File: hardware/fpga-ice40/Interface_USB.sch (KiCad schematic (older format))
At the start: 12 parts, among them J5 USB_B_Micro, U7 FT245RL

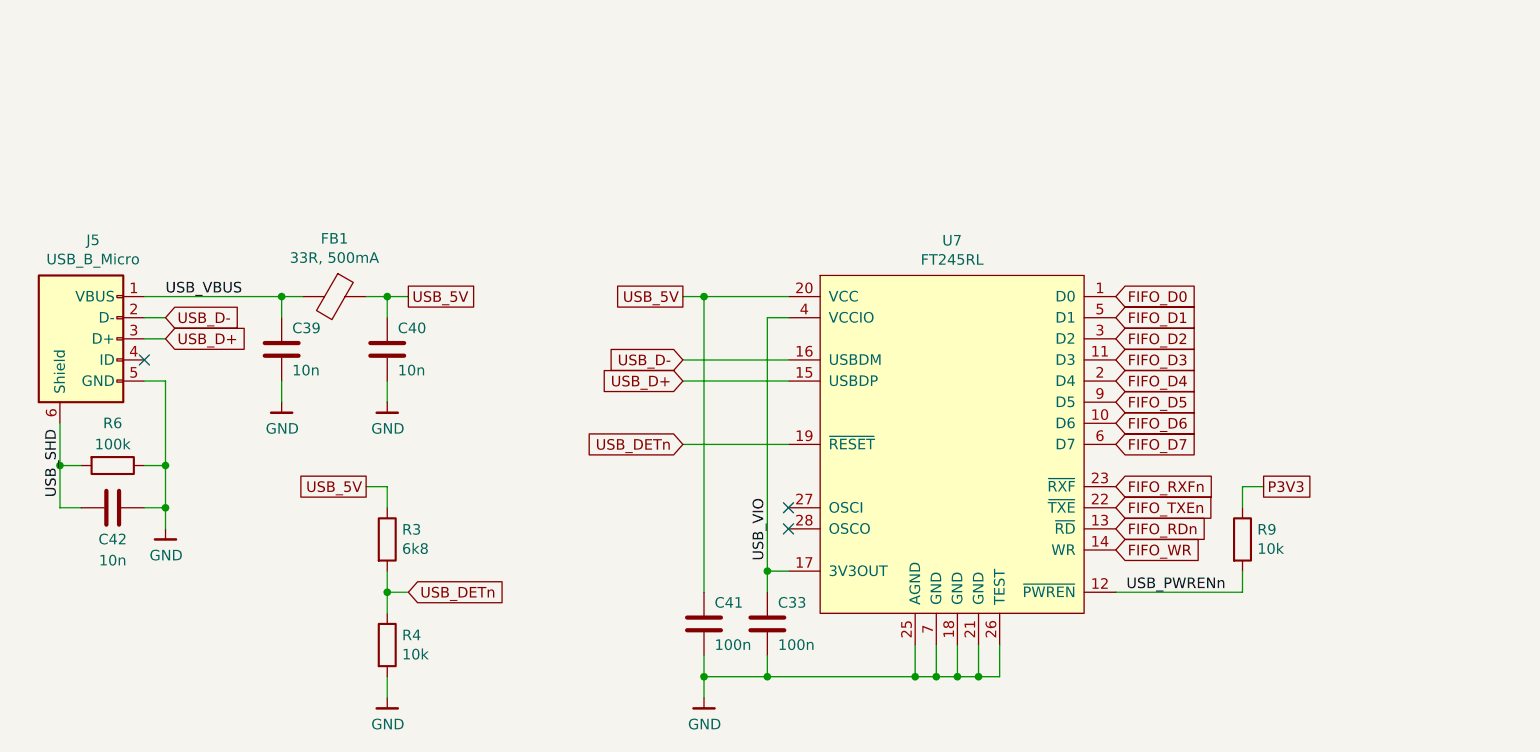
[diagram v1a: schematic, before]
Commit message: Reannotate schematic symbols
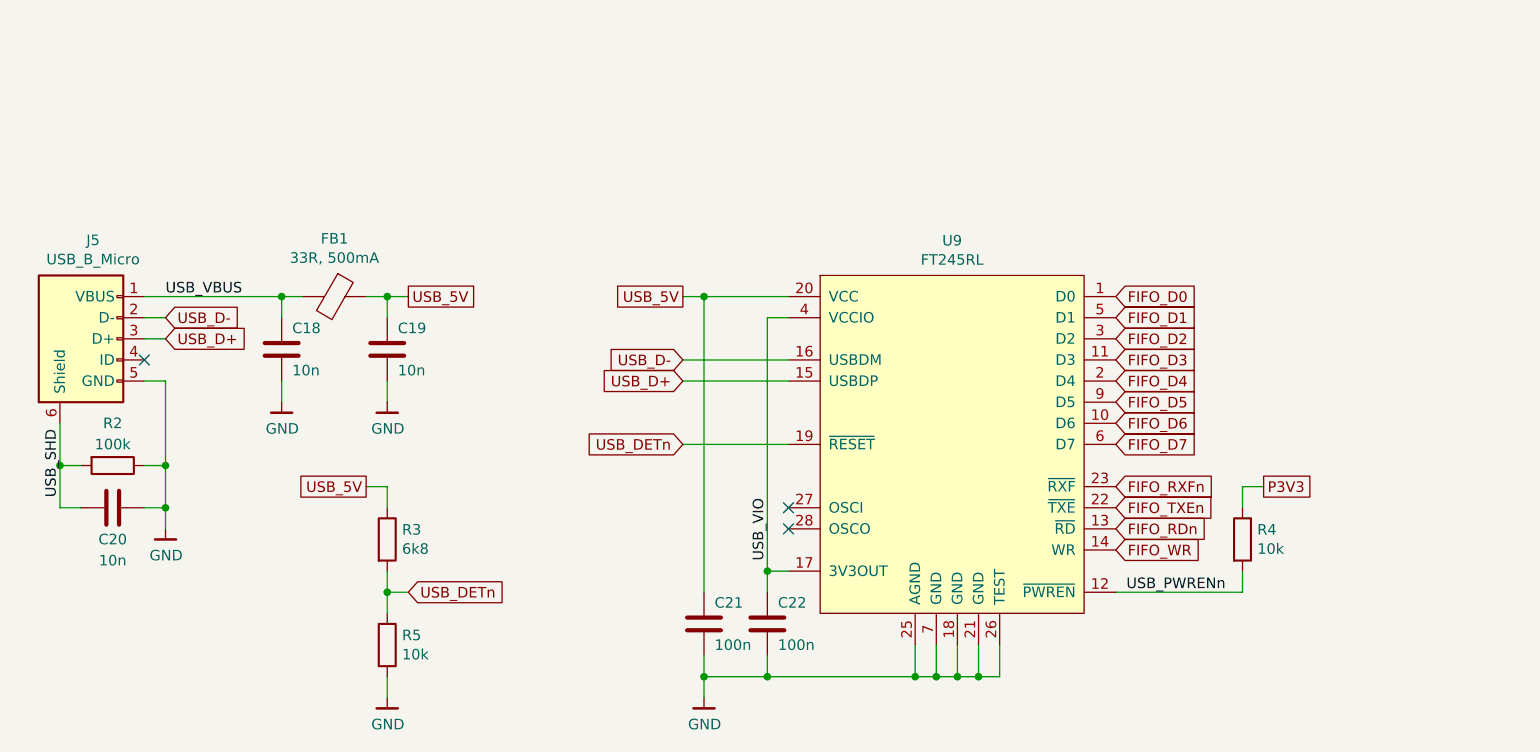
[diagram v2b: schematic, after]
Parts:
- renumbered C39 to C18, C40 to C19, C42 to C20, C41 to C21, C33 to C22, R6 to R2, R9 to R4, R4 to R5, U7 to U9
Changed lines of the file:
@@
 P 6350 3750
 AR Path="/5F314850" Ref="U?"  Part="1"
-AR Path="/5F302051/5F314850" Ref="U7"  Part="1"
-F 0 "U7" H 6975 4315 50  0000 C CNN
+AR Path="/5F302051/5F314850" Ref="U9"  Part="1"
+F 0 "U9" H 6975 4315 50  0000 C CNN
 F 1 "FT245RL" H 6975 4224 50  0000 C CNN
 F 2 "Package_SO:SSOP-28_5.3x10.2mm_P0.65mm" H 6500 4200 50  0001 C CNN
@@
 P 5800 5350
 AR Path="/5F314866" Ref="#PWR?"  Part="1"
-AR Path="/5F302051/5F314866" Ref="#PWR0121"  Part="1"
-F 0 "#PWR0121" H 5800 5100 50  0001 C CNN
+AR Path="/5F302051/5F314866" Ref="#PWR025"  Part="1"
+F 0 "#PWR025" H 5800 5100 50  0001 C CNN
 F 1 "GND" H 5803 5224 50  0000 C CNN
 F 2 "" H 5700 5000 50  0001 C CNN
@@
 P 6100 5000
 AR Path="/5F31486F" Ref="C?"  Part="1"
-AR Path="/5F302051/5F31486F" Ref="C33"  Part="1"
-F 0 "C33" H 6150 5100 50  0000 L CNN
+AR Path="/5F302051/5F31486F" Ref="C22"  Part="1"
+F 0 "C22" H 6150 5100 50  0000 L CNN
 F 1 "100n" H 6150 4900 50  0000 L CNN
 F 2 "Capacitor_SMD:C_0603_1608Metric" H 6138 4850 50  0001 C CNN
@@
 P 8350 4600
 AR Path="/5F314883" Ref="R?"  Part="1"
-AR Path="/5F302051/5F314883" Ref="R9"  Part="1"
-F 0 "R9" H 8420 4646 50  0000 L CNN
+AR Path="/5F302051/5F314883" Ref="R4"  Part="1"
+F 0 "R4" H 8420 4646 50  0000 L CNN
 F 1 "10k" H 8420 4555 50  0000 L CNN
 F 2 "Resistor_SMD:R_0603_1608Metric" V 8280 4600 50  0001 C CNN
@@
 P 3250 4550
 AR Path="/5F3148A5" Ref="#PWR?"  Part="1"
-AR Path="/5F302051/5F3148A5" Ref="#PWR0122"  Part="1"
-F 0 "#PWR0122" H 3250 4300 50  0001 C CNN
+AR Path="/5F302051/5F3148A5" Ref="#PWR023"  Part="1"
+F 0 "#PWR023" H 3250 4300 50  0001 C CNN
 F 1 "GND" H 3253 4424 50  0000 C CNN
 F 2 "" H 3150 4200 50  0001 C CNN
@@
 P 4300 5100
 AR Path="/5F3148B3" Ref="R?"  Part="1"
-AR Path="/5F302051/5F3148B3" Ref="R4"  Part="1"
-F 0 "R4" H 4370 5146 50  0000 L CNN
+AR Path="/5F302051/5F3148B3" Ref="R5"  Part="1"
+F 0 "R5" H 4370 5146 50  0000 L CNN
 F 1 "10k" H 4370 5055 50  0000 L CNN
 F 2 "Resistor_SMD:R_0603_1608Metric" V 4230 5100 50  0001 C CNN
@@
 P 4300 5350
 AR Path="/5F3148BA" Ref="#PWR?"  Part="1"
-AR Path="/5F302051/5F3148BA" Ref="#PWR0123"  Part="1"
-F 0 "#PWR0123" H 4300 5100 50  0001 C CNN
+AR Path="/5F302051/5F3148BA" Ref="#PWR024"  Part="1"
+F 0 "#PWR024" H 4300 5100 50  0001 C CNN
 F 1 "GND" H 4303 5224 50  0000 C CNN
 F 2 "" H 4200 5000 50  0001 C CNN
@@
 P 5800 5000
 AR Path="/5F3148C7" Ref="C?"  Part="1"
-AR Path="/5F302051/5F3148C7" Ref="C41"  Part="1"
-F 0 "C41" H 5850 5100 50  0000 L CNN
+AR Path="/5F302051/5F3148C7" Ref="C21"  Part="1"
+F 0 "C21" H 5850 5100 50  0000 L CNN
 F 1 "100n" H 5850 4900 50  0000 L CNN
 F 2 "Capacitor_SMD:C_0603_1608Metric" H 5838 4850 50  0001 C CNN
@@
 P 3800 3700
 AR Path="/5F3148D5" Ref="C?"  Part="1"
-AR Path="/5F302051/5F3148D5" Ref="C39"  Part="1"
-F 0 "C39" H 3850 3800 50  0000 L CNN
+AR Path="/5F302051/5F3148D5" Ref="C18"  Part="1"
+F 0 "C18" H 3850 3800 50  0000 L CNN
 F 1 "10n" H 3850 3600 50  0000 L CNN
 F 2 "Capacitor_SMD:C_0603_1608Metric" H 3838 3550 50  0001 C CNN
@@
 P 3800 3950
 AR Path="/5F3148DE" Ref="#PWR?"  Part="1"
-AR Path="/5F302051/5F3148DE" Ref="#PWR0124"  Part="1"
-F 0 "#PWR0124" H 3800 3700 50  0001 C CNN
+AR Path="/5F302051/5F3148DE" Ref="#PWR021"  Part="1"
+F 0 "#PWR021" H 3800 3700 50  0001 C CNN
 F 1 "GND" H 3803 3824 50  0000 C CNN
 F 2 "" H 3700 3600 50  0001 C CNN
@@
 P 4300 3700
 AR Path="/5F3148ED" Ref="C?"  Part="1"
-AR Path="/5F302051/5F3148ED" Ref="C40"  Part="1"
-F 0 "C40" H 4350 3800 50  0000 L CNN
+AR Path="/5F302051/5F3148ED" Ref="C19"  Part="1"
+F 0 "C19" H 4350 3800 50  0000 L CNN
 F 1 "10n" H 4350 3600 50  0000 L CNN
 F 2 "Capacitor_SMD:C_0603_1608Metric" H 4338 3550 50  0001 C CNN
@@
 P 4300 3950
 AR Path="/5F3148F5" Ref="#PWR?"  Part="1"
-AR Path="/5F302051/5F3148F5" Ref="#PWR0125"  Part="1"
-F 0 "#PWR0125" H 4300 3700 50  0001 C CNN
+AR Path="/5F302051/5F3148F5" Ref="#PWR022"  Part="1"
+F 0 "#PWR022" H 4300 3700 50  0001 C CNN
 F 1 "GND" H 4303 3824 50  0000 C CNN
 F 2 "" H 4200 3600 50  0001 C CNN
@@
 P 3000 4250
 AR Path="/5F314900" Ref="R?"  Part="1"
-AR Path="/5F302051/5F314900" Ref="R6"  Part="1"
-F 0 "R6" V 2800 4250 50  0000 C CNN
+AR Path="/5F302051/5F314900" Ref="R2"  Part="1"
+F 0 "R2" V 2800 4250 50  0000 C CNN
 F 1 "100k" V 2900 4250 50  0000 C CNN
 F 2 "Resistor_SMD:R_0603_1608Metric" V 2930 4250 50  0001 C CNN
@@
 P 3000 4450
 AR Path="/5F314906" Ref="C?"  Part="1"
-AR Path="/5F302051/5F314906" Ref="C42"  Part="1"
-F 0 "C42" V 2850 4450 50  0000 C CNN
+AR Path="/5F302051/5F314906" Ref="C20"  Part="1"
+F 0 "C20" V 2850 4450 50  0000 C CNN
 F 1 "10n" V 2750 4450 50  0000 C CNN
 F 2 "Capacitor_SMD:C_0603_1608Metric" H 3038 4300 50  0001 C CNN

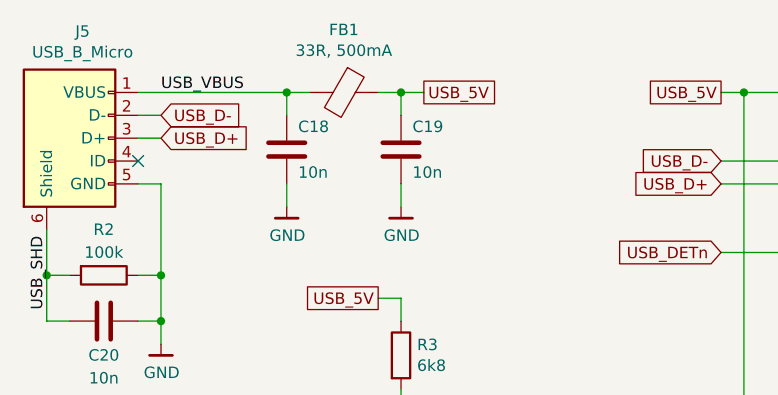
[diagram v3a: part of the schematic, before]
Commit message: Component selection by MPN and routing cleanup
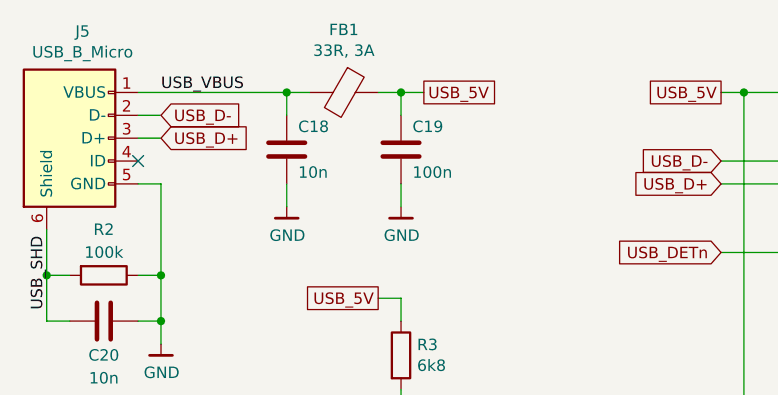
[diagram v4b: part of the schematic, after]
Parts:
- C18, C20: MPN (none) -> CL10B103KC8NNNC
- C19: value 10n -> 100n; MPN (none) -> CL10B104KB8NNNC
- C21, C22: MPN (none) -> CL10B104KB8NNNC
- FB1: value 33R, 500mA -> 33R, 3A; MPN 742792605 -> BLM18PG330SN1D
- J5: MPN (none) -> 47346-0001
- U9: MPN (none) -> FT245RL-REEL
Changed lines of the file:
@@
 F 2 "Package_SO:SSOP-28_5.3x10.2mm_P0.65mm" H 6500 4200 50  0001 C CNN
 F 3 "https://www.ftdichip.com/Support/Documents/DataSheets/ICs/DS_FT245R.pdf" H 6500 4200 50  0001 C CNN
+F 4 "FT245RL-REEL" H 6350 3750 50  0001 C CNN "MPN"
 	1    6350 3750
 	1    0    0    -1
@@
 F 2 "Capacitor_SMD:C_0603_1608Metric" H 6138 4850 50  0001 C CNN
 F 3 "~" H 6100 5000 50  0001 C CNN
+F 4 "CL10B104KB8NNNC" H 6100 5000 50  0001 C CNN "MPN"
 	1    6100 5000
 	1    0    0    -1
@@
 Text Label 7800 4850 0    50   ~ 0
 USB_PWRENn
-NoConn ~ 3150 3750
-Wire Wire Line
-	3150 3850 3250 3850
-Wire Wire Line
-	3250 3850 3250 4250
-Wire Wire Line
-	3150 3450 3800 3450
-Wire Wire Line
-	3150 3550 3250 3550
-Wire Wire Line
-	3150 3650 3250 3650
-$Comp
-L ng_power:GND #PWR?
-U 1 1 5F3148A5
-P 3250 4550
-AR Path="/5F3148A5" Ref="#PWR?"  Part="1"
-AR Path="/5F302051/5F3148A5" Ref="#PWR023"  Part="1"
-F 0 "#PWR023" H 3250 4300 50  0001 C CNN
-F 1 "GND" H 3253 4424 50  0000 C CNN
-F 2 "" H 3150 4200 50  0001 C CNN
-F 3 "" H 3250 4550 50  0001 C CNN
-	1    3250 4550
-	1    0    0    -1
-$EndComp
-Text GLabel 3250 3550 2    50   Input ~ 0
-USB_D-
-Text GLabel 3250 3650 2    50   Input ~ 0
-USB_D+
 $Comp
 L Device:R R?
@@
 F 2 "Capacitor_SMD:C_0603_1608Metric" H 5838 4850 50  0001 C CNN
 F 3 "~" H 5800 5000 50  0001 C CNN
+F 4 "CL10B104KB8NNNC" H 5800 5000 50  0001 C CNN "MPN"
 	1    5800 5000
 	1    0    0    -1
@@
 F 2 "Capacitor_SMD:C_0603_1608Metric" H 3838 3550 50  0001 C CNN
 F 3 "~" H 3800 3700 50  0001 C CNN
+F 4 "CL10B103KC8NNNC" H 3800 3700 50  0001 C CNN "MPN"
 	1    3800 3700
 	1    0    0    -1
 $EndComp
-Text Label 3250 3450 0    50   ~ 0
-USB_VBUS
 Wire Wire Line
 	3800 3450 3800 3550
@@
 AR Path="/5F302051/5F3148E5" Ref="FB1"  Part="1"
 F 0 "FB1" V 3776 3450 50  0000 C CNN
-F 1 "33R, 500mA" V 3867 3450 50  0000 C CNN
+F 1 "33R, 3A" V 3867 3450 50  0000 C CNN
 F 2 "Inductor_SMD:L_0603_1608Metric" V 3980 3450 50  0001 C CNN
 F 3 "~" H 4050 3450 50  0001 C CNN
-F 4 "742792605" V 4050 3450 50  0001 C CNN "MPN"
+F 4 "BLM18PG330SN1D" V 4050 3450 50  0001 C CNN "MPN"
 	1    4050 3450
 	0    1    1    0
@@
 Wire Wire Line
 	3900 3450 3800 3450
-Connection ~ 3800 3450
 $Comp
 L Device:C C?
@@
 AR Path="/5F302051/5F3148ED" Ref="C19"  Part="1"
 F 0 "C19" H 4350 3800 50  0000 L CNN
-F 1 "10n" H 4350 3600 50  0000 L CNN
+F 1 "100n" H 4350 3600 50  0000 L CNN
 F 2 "Capacitor_SMD:C_0603_1608Metric" H 4338 3550 50  0001 C CNN
 F 3 "~" H 4300 3700 50  0001 C CNN
+F 4 "CL10B104KB8NNNC" H 4300 3700 50  0001 C CNN "MPN"
 	1    4300 3700
 	1    0    0    -1
@@
 Text GLabel 4200 4350 0    50   UnSpc ~ 0
 USB_5V
+Connection ~ 3800 3450
+$Comp
+L ng_conn:USB_B_Micro J?
+U 1 1 5F314899
+P 2850 3650
+AR Path="/5F314899" Ref="J?"  Part="1"
+AR Path="/5F302051/5F314899" Ref="J5"  Part="1"
+F 0 "J5" H 2907 4117 50  0000 C CNN
+F 1 "USB_B_Micro" H 2907 4026 50  0000 C CNN
+F 2 "Connector_USB:USB_Micro-B_Molex_47346-0001" H 3000 3650 50  0001 C CNN
+F 3 "~" H 3000 3650 50  0001 C CNN
+F 4 "47346-0001" H 2850 3650 50  0001 C CNN "MPN"
+	1    2850 3650
+	1    0    0    -1
+$EndComp
+Text Label 2750 4400 1    50   ~ 0
+USB_SHD
+Connection ~ 2750 4250
+Wire Wire Line
+	2750 4450 2750 4250
+Wire Wire Line
+	2850 4450 2750 4450
+Wire Wire Line
+	2750 4250 2750 4050
+Wire Wire Line
+	2850 4250 2750 4250
+Wire Wire Line
+	3250 4450 3250 4550
+Connection ~ 3250 4450
+Wire Wire Line
+	3150 4450 3250 4450
+Wire Wire Line
+	3250 4250 3250 4450
+Connection ~ 3250 4250
+Wire Wire Line
+	3150 4250 3250 4250
+$Comp
+L Device:C C?
+U 1 1 5F314906
+P 3000 4450
+AR Path="/5F314906" Ref="C?"  Part="1"
+AR Path="/5F302051/5F314906" Ref="C20"  Part="1"
+F 0 "C20" V 2850 4450 50  0000 C CNN
+F 1 "10n" V 2750 4450 50  0000 C CNN
+F 2 "Capacitor_SMD:C_0603_1608Metric" H 3038 4300 50  0001 C CNN
+F 3 "~" H 3000 4450 50  0001 C CNN
+F 4 "CL10B103KC8NNNC" H 3000 4450 50  0001 C CNN "MPN"
+	1    3000 4450
+	0    -1   -1   0
+$EndComp
 $Comp
 L Device:R R?
@@
 	0    1    1    0
 $EndComp
-$Comp
-L Device:C C?
-U 1 1 5F314906
-P 3000 4450
-AR Path="/5F314906" Ref="C?"  Part="1"
-AR Path="/5F302051/5F314906" Ref="C20"  Part="1"
-F 0 "C20" V 2850 4450 50  0000 C CNN
-F 1 "10n" V 2750 4450 50  0000 C CNN
-F 2 "Capacitor_SMD:C_0603_1608Metric" H 3038 4300 50  0001 C CNN
-F 3 "~" H 3000 4450 50  0001 C CNN
-	1    3000 4450
-	0    -1   -1   0
-$EndComp
-Wire Wire Line
-	3150 4250 3250 4250
-Connection ~ 3250 4250
-Wire Wire Line
-	3250 4250 3250 4450
-Wire Wire Line
-	3150 4450 3250 4450
-Connection ~ 3250 4450
-Wire Wire Line
-	3250 4450 3250 4550
-Wire Wire Line
-	2850 4250 2750 4250
-Wire Wire Line
-	2750 4250 2750 4050
-Wire Wire Line
-	2850 4450 2750 4450
-Wire Wire Line
-	2750 4450 2750 4250
-Connection ~ 2750 4250
-Text Label 2750 4400 1    50   ~ 0
-USB_SHD
-$Comp
-L ng_conn:USB_B_Micro J?
-U 1 1 5F314899
-P 2850 3650
-AR Path="/5F314899" Ref="J?"  Part="1"
-AR Path="/5F302051/5F314899" Ref="J5"  Part="1"
-F 0 "J5" H 2907 4117 50  0000 C CNN
-F 1 "USB_B_Micro" H 2907 4026 50  0000 C CNN
-F 2 "Connector_USB:USB_Micro-B_Molex_47346-0001" H 3000 3650 50  0001 C CNN
-F 3 "~" H 3000 3650 50  0001 C CNN
-	1    2850 3650
-	1    0    0    -1
-$EndComp
+Text Label 3250 3450 0    50   ~ 0
+USB_VBUS
+Text GLabel 3250 3650 2    50   Input ~ 0
+USB_D+
+Text GLabel 3250 3550 2    50   Input ~ 0
+USB_D-
+$Comp
+L ng_power:GND #PWR?
+U 1 1 5F3148A5
+P 3250 4550
+AR Path="/5F3148A5" Ref="#PWR?"  Part="1"
+AR Path="/5F302051/5F3148A5" Ref="#PWR023"  Part="1"
+F 0 "#PWR023" H 3250 4300 50  0001 C CNN
+F 1 "GND" H 3253 4424 50  0000 C CNN
+F 2 "" H 3150 4200 50  0001 C CNN
+F 3 "" H 3250 4550 50  0001 C CNN
+	1    3250 4550
+	1    0    0    -1
+$EndComp
+Wire Wire Line
+	3150 3650 3250 3650
+Wire Wire Line
+	3150 3550 3250 3550
+Wire Wire Line
+	3150 3450 3800 3450
+Wire Wire Line
+	3250 3850 3250 4250
+Wire Wire Line
+	3150 3850 3250 3850
+NoConn ~ 3150 3750
 $EndSCHEMATC

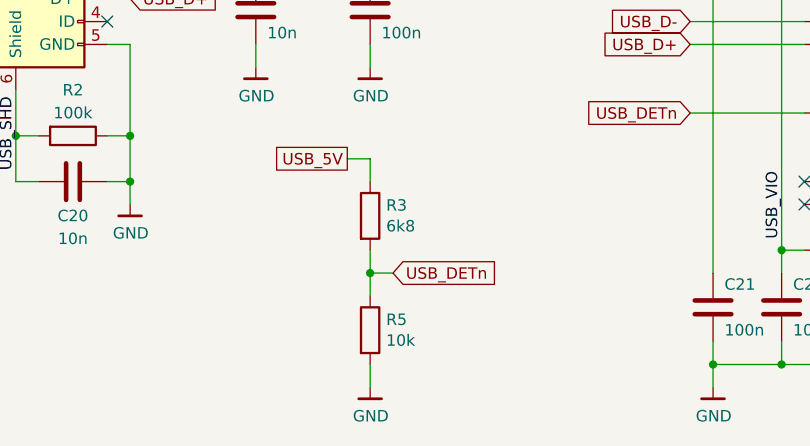
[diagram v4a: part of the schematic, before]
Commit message: Complete component selection by MPN
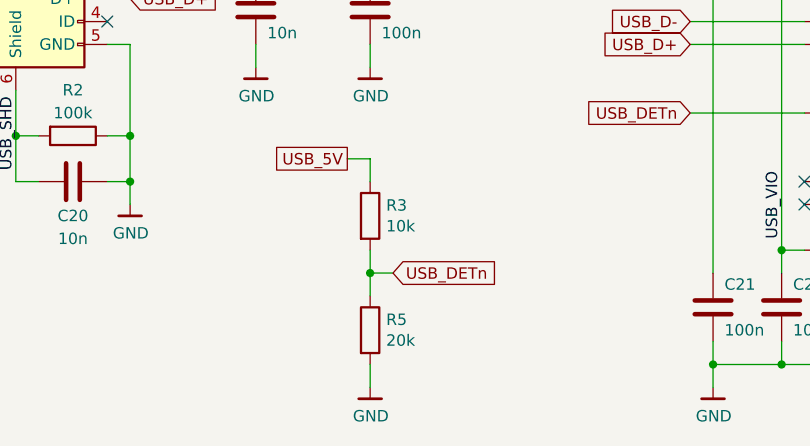
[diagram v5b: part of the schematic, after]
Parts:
- R2: MPN (none) -> RC0603JR-07100KL
- R3: value 6k8 -> 10k; MPN (none) -> RC0603FR-0710KL
- R4: MPN (none) -> RC0603FR-0710KL
- R5: value 10k -> 20k; MPN (none) -> RC0603JR-0720KL
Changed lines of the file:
@@
 F 2 "Resistor_SMD:R_0603_1608Metric" V 8280 4600 50  0001 C CNN
 F 3 "~" H 8350 4600 50  0001 C CNN
+F 4 "RC0603FR-0710KL" H 8350 4600 50  0001 C CNN "MPN"
 	1    8350 4600
 	1    0    0    -1
@@
 AR Path="/5F302051/5F3148AD" Ref="R3"  Part="1"
 F 0 "R3" H 4370 4646 50  0000 L CNN
-F 1 "6k8" H 4370 4555 50  0000 L CNN
+F 1 "10k" H 4370 4555 50  0000 L CNN
 F 2 "Resistor_SMD:R_0603_1608Metric" V 4230 4600 50  0001 C CNN
 F 3 "~" H 4300 4600 50  0001 C CNN
+F 4 "RC0603FR-0710KL" H 4300 4600 50  0001 C CNN "MPN"
 	1    4300 4600
 	1    0    0    -1
@@
 AR Path="/5F302051/5F3148B3" Ref="R5"  Part="1"
 F 0 "R5" H 4370 5146 50  0000 L CNN
-F 1 "10k" H 4370 5055 50  0000 L CNN
+F 1 "20k" H 4370 5055 50  0000 L CNN
 F 2 "Resistor_SMD:R_0603_1608Metric" V 4230 5100 50  0001 C CNN
 F 3 "~" H 4300 5100 50  0001 C CNN
+F 4 "RC0603JR-0720KL" H 4300 5100 50  0001 C CNN "MPN"
 	1    4300 5100
 	1    0    0    -1
@@
 F 2 "Resistor_SMD:R_0603_1608Metric" V 2930 4250 50  0001 C CNN
 F 3 "~" H 3000 4250 50  0001 C CNN
+F 4 "RC0603JR-07100KL" H 3000 4250 50  0001 C CNN "MPN"
 	1    3000 4250
 	0    1    1    0
